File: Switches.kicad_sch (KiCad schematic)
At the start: 26 parts, among them Q10 POWER_FET, Q11 POWER_FET, Q12 POWER_FET, Q7 POWER_FET, Q8 POWER_FET, Q9 POWER_FET

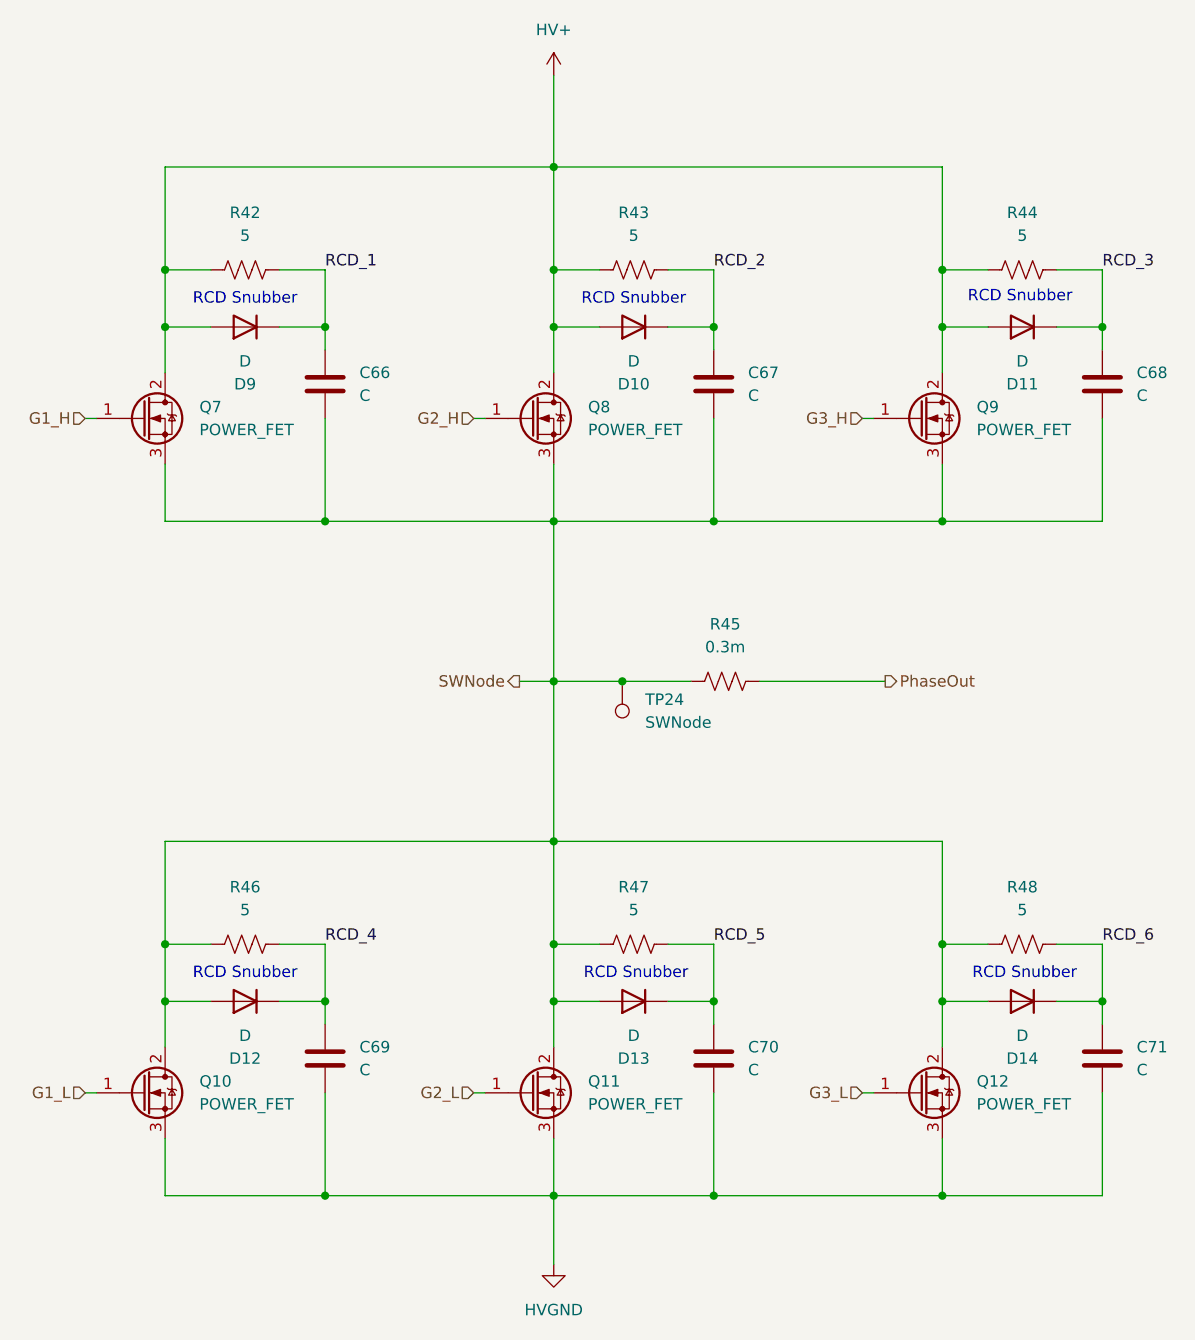
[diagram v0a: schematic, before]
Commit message: new bulk caps, new HV+,- connector placement
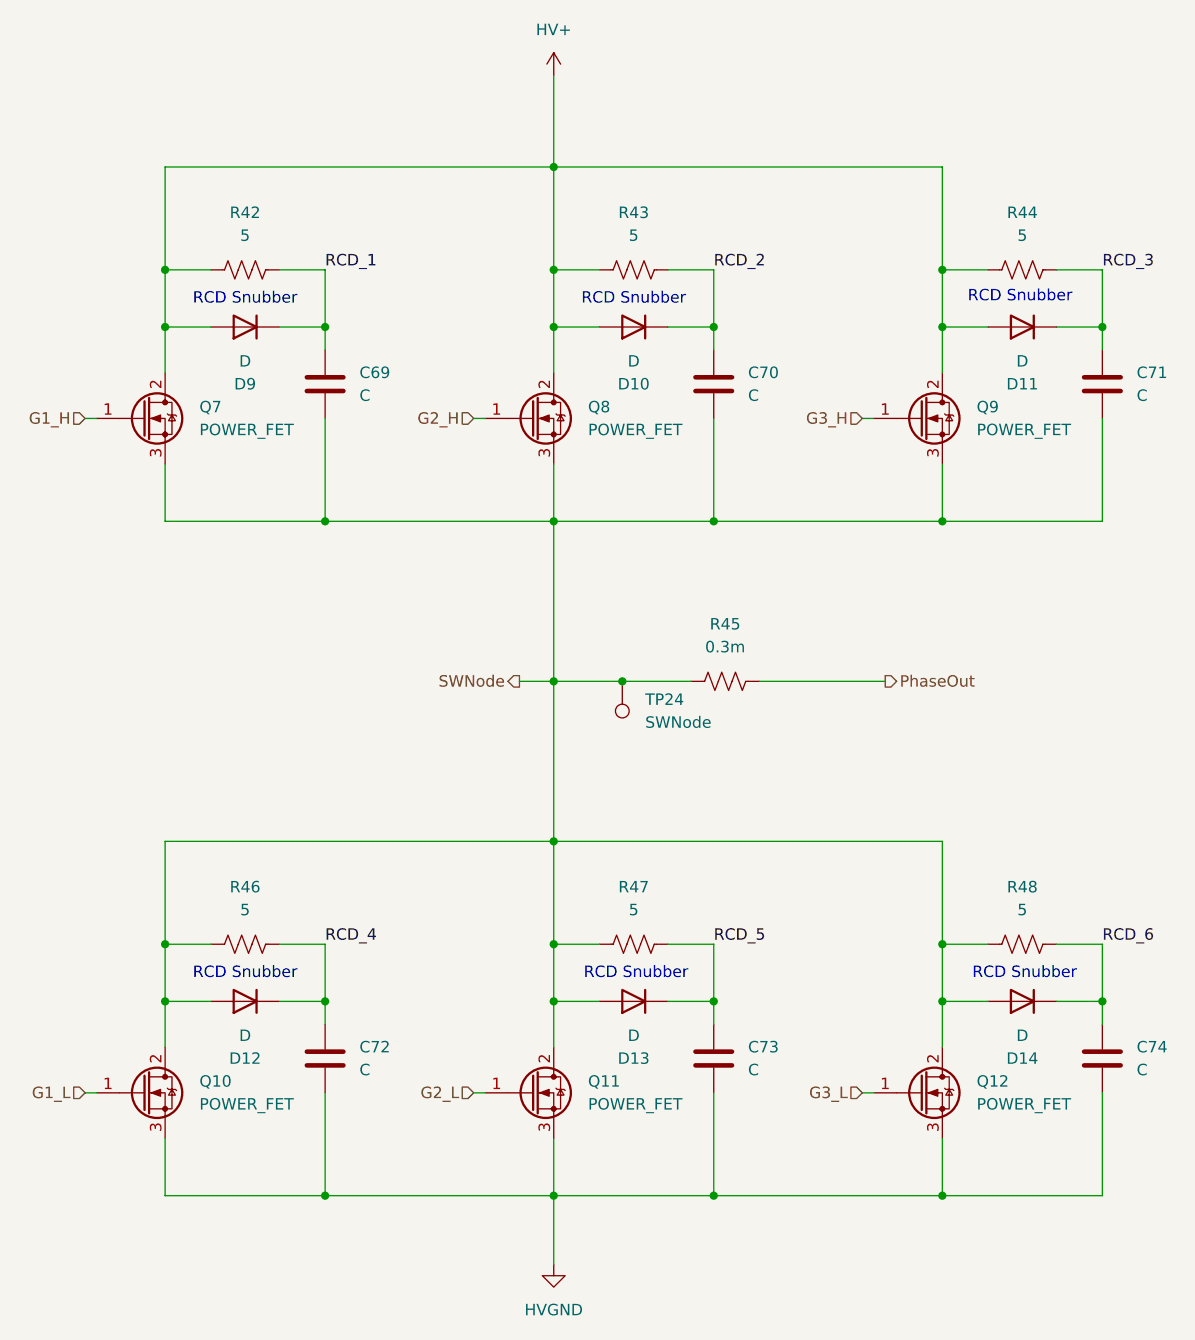
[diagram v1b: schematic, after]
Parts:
- renumbered C66 to C69, C67 to C70, C68 to C71, C69 to C72, C70 to C73, C71 to C74
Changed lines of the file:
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@@
 				)
 				(path "/bc91ffbf-afc6-42bb-9d28-6a3fecc21fcc/ebf1904e-ffdd-4ce1-98fa-2546468af80b/8a53f8a7-4fee-45b0-8115-af4354d69d86/61f5303a-4fdd-407b-8b75-bd44ef1dd029"
-					(reference "#PWR0175")
-					(unit 1)
-				)
-				(path "/bc91ffbf-afc6-42bb-9d28-6a3fecc21fcc/f1a23dc8-fe65-401e-b36f-fdc2d19203b3/8a53f8a7-4fee-45b0-8115-af4354d69d86/61f5303a-4fdd-407b-8b75-bd44ef1dd029"
-					(reference "#PWR0104")
+					(reference "#PWR0163")
+					(unit 1)
+				)
+				(path "/bc91ffbf-afc6-42bb-9d28-6a3fecc21fcc/f1a23dc8-fe65-401e-b36f-fdc2d19203b3/8a53f8a7-4fee-45b0-8115-af4354d69d86/61f5303a-4fdd-407b-8b75-bd44ef1dd029"
+					(reference "#PWR098")
 					(unit 1)
 				)
@@
 				)
 				(path "/bc91ffbf-afc6-42bb-9d28-6a3fecc21fcc/ebf1904e-ffdd-4ce1-98fa-2546468af80b/8a53f8a7-4fee-45b0-8115-af4354d69d86/61f5303a-4fdd-407b-8b75-bd44ef1dd029"
-					(reference "#PWR0176")
-					(unit 1)
-				)
-				(path "/bc91ffbf-afc6-42bb-9d28-6a3fecc21fcc/f1a23dc8-fe65-401e-b36f-fdc2d19203b3/8a53f8a7-4fee-45b0-8115-af4354d69d86/61f5303a-4fdd-407b-8b75-bd44ef1dd029"
-					(reference "#PWR0105")
+					(reference "#PWR0164")
+					(unit 1)
+				)
+				(path "/bc91ffbf-afc6-42bb-9d28-6a3fecc21fcc/f1a23dc8-fe65-401e-b36f-fdc2d19203b3/8a53f8a7-4fee-45b0-8115-af4354d69d86/61f5303a-4fdd-407b-8b75-bd44ef1dd029"
+					(reference "#PWR099")
 					(unit 1)
 				)
@@
 		(dnp no)
 		(fields_autoplaced yes)
-		(property "Reference" "C67"
+		(property "Reference" "C70"
 			(at 157.48 62.2299 0)
 			(effects
@@
 			(project "TractionInverter"
 				(path "/bc91ffbf-afc6-42bb-9d28-6a3fecc21fcc/3f7f1099-e875-4a86-860c-ef7a3936f734/8a53f8a7-4fee-45b0-8115-af4354d69d86/61f5303a-4fdd-407b-8b75-bd44ef1dd029"
-					(reference "C67")
-					(unit 1)
-				)
-				(path "/bc91ffbf-afc6-42bb-9d28-6a3fecc21fcc/ebf1904e-ffdd-4ce1-98fa-2546468af80b/8a53f8a7-4fee-45b0-8115-af4354d69d86/61f5303a-4fdd-407b-8b75-bd44ef1dd029"
-					(reference "C121")
-					(unit 1)
-				)
-				(path "/bc91ffbf-afc6-42bb-9d28-6a3fecc21fcc/f1a23dc8-fe65-401e-b36f-fdc2d19203b3/8a53f8a7-4fee-45b0-8115-af4354d69d86/61f5303a-4fdd-407b-8b75-bd44ef1dd029"
-					(reference "C75")
+					(reference "C70")
+					(unit 1)
+				)
+				(path "/bc91ffbf-afc6-42bb-9d28-6a3fecc21fcc/ebf1904e-ffdd-4ce1-98fa-2546468af80b/8a53f8a7-4fee-45b0-8115-af4354d69d86/61f5303a-4fdd-407b-8b75-bd44ef1dd029"
+					(reference "C124")
+					(unit 1)
+				)
+				(path "/bc91ffbf-afc6-42bb-9d28-6a3fecc21fcc/f1a23dc8-fe65-401e-b36f-fdc2d19203b3/8a53f8a7-4fee-45b0-8115-af4354d69d86/61f5303a-4fdd-407b-8b75-bd44ef1dd029"
+					(reference "C78")
 					(unit 1)
 				)
@@
 		(dnp no)
 		(fields_autoplaced yes)
-		(property "Reference" "C69"
+		(property "Reference" "C72"
 			(at 114.3 137.1599 0)
 			(effects
@@
 			(project "TractionInverter"
 				(path "/bc91ffbf-afc6-42bb-9d28-6a3fecc21fcc/3f7f1099-e875-4a86-860c-ef7a3936f734/8a53f8a7-4fee-45b0-8115-af4354d69d86/61f5303a-4fdd-407b-8b75-bd44ef1dd029"
-					(reference "C69")
-					(unit 1)
-				)
-				(path "/bc91ffbf-afc6-42bb-9d28-6a3fecc21fcc/ebf1904e-ffdd-4ce1-98fa-2546468af80b/8a53f8a7-4fee-45b0-8115-af4354d69d86/61f5303a-4fdd-407b-8b75-bd44ef1dd029"
-					(reference "C123")
-					(unit 1)
-				)
-				(path "/bc91ffbf-afc6-42bb-9d28-6a3fecc21fcc/f1a23dc8-fe65-401e-b36f-fdc2d19203b3/8a53f8a7-4fee-45b0-8115-af4354d69d86/61f5303a-4fdd-407b-8b75-bd44ef1dd029"
-					(reference "C77")
+					(reference "C72")
+					(unit 1)
+				)
+				(path "/bc91ffbf-afc6-42bb-9d28-6a3fecc21fcc/ebf1904e-ffdd-4ce1-98fa-2546468af80b/8a53f8a7-4fee-45b0-8115-af4354d69d86/61f5303a-4fdd-407b-8b75-bd44ef1dd029"
+					(reference "C126")
+					(unit 1)
+				)
+				(path "/bc91ffbf-afc6-42bb-9d28-6a3fecc21fcc/f1a23dc8-fe65-401e-b36f-fdc2d19203b3/8a53f8a7-4fee-45b0-8115-af4354d69d86/61f5303a-4fdd-407b-8b75-bd44ef1dd029"
+					(reference "C80")
 					(unit 1)
 				)
@@
 		(dnp no)
 		(fields_autoplaced yes)
-		(property "Reference" "C71"
+		(property "Reference" "C74"
 			(at 200.66 137.1599 0)
 			(effects
@@
 			(project "TractionInverter"
 				(path "/bc91ffbf-afc6-42bb-9d28-6a3fecc21fcc/3f7f1099-e875-4a86-860c-ef7a3936f734/8a53f8a7-4fee-45b0-8115-af4354d69d86/61f5303a-4fdd-407b-8b75-bd44ef1dd029"
-					(reference "C71")
-					(unit 1)
-				)
-				(path "/bc91ffbf-afc6-42bb-9d28-6a3fecc21fcc/ebf1904e-ffdd-4ce1-98fa-2546468af80b/8a53f8a7-4fee-45b0-8115-af4354d69d86/61f5303a-4fdd-407b-8b75-bd44ef1dd029"
-					(reference "C125")
-					(unit 1)
-				)
-				(path "/bc91ffbf-afc6-42bb-9d28-6a3fecc21fcc/f1a23dc8-fe65-401e-b36f-fdc2d19203b3/8a53f8a7-4fee-45b0-8115-af4354d69d86/61f5303a-4fdd-407b-8b75-bd44ef1dd029"
-					(reference "C79")
+					(reference "C74")
+					(unit 1)
+				)
+				(path "/bc91ffbf-afc6-42bb-9d28-6a3fecc21fcc/ebf1904e-ffdd-4ce1-98fa-2546468af80b/8a53f8a7-4fee-45b0-8115-af4354d69d86/61f5303a-4fdd-407b-8b75-bd44ef1dd029"
+					(reference "C128")
+					(unit 1)
+				)
+				(path "/bc91ffbf-afc6-42bb-9d28-6a3fecc21fcc/f1a23dc8-fe65-401e-b36f-fdc2d19203b3/8a53f8a7-4fee-45b0-8115-af4354d69d86/61f5303a-4fdd-407b-8b75-bd44ef1dd029"
+					(reference "C82")
 					(unit 1)
 				)
@@
 		(dnp no)
 		(fields_autoplaced yes)
-		(property "Reference" "C68"
+		(property "Reference" "C71"
 			(at 200.66 62.2299 0)
 			(effects
@@
 			(project "TractionInverter"
 				(path "/bc91ffbf-afc6-42bb-9d28-6a3fecc21fcc/3f7f1099-e875-4a86-860c-ef7a3936f734/8a53f8a7-4fee-45b0-8115-af4354d69d86/61f5303a-4fdd-407b-8b75-bd44ef1dd029"
-					(reference "C68")
-					(unit 1)
-				)
-				(path "/bc91ffbf-afc6-42bb-9d28-6a3fecc21fcc/ebf1904e-ffdd-4ce1-98fa-2546468af80b/8a53f8a7-4fee-45b0-8115-af4354d69d86/61f5303a-4fdd-407b-8b75-bd44ef1dd029"
-					(reference "C122")
-					(unit 1)
-				)
-				(path "/bc91ffbf-afc6-42bb-9d28-6a3fecc21fcc/f1a23dc8-fe65-401e-b36f-fdc2d19203b3/8a53f8a7-4fee-45b0-8115-af4354d69d86/61f5303a-4fdd-407b-8b75-bd44ef1dd029"
-					(reference "C76")
+					(reference "C71")
+					(unit 1)
+				)
+				(path "/bc91ffbf-afc6-42bb-9d28-6a3fecc21fcc/ebf1904e-ffdd-4ce1-98fa-2546468af80b/8a53f8a7-4fee-45b0-8115-af4354d69d86/61f5303a-4fdd-407b-8b75-bd44ef1dd029"
+					(reference "C125")
+					(unit 1)
+				)
+				(path "/bc91ffbf-afc6-42bb-9d28-6a3fecc21fcc/f1a23dc8-fe65-401e-b36f-fdc2d19203b3/8a53f8a7-4fee-45b0-8115-af4354d69d86/61f5303a-4fdd-407b-8b75-bd44ef1dd029"
+					(reference "C79")
 					(unit 1)
 				)
@@
 		(dnp no)
 		(fields_autoplaced yes)
-		(property "Reference" "C66"
+		(property "Reference" "C69"
 			(at 114.3 62.2299 0)
 			(effects
@@
 			(project "TractionInverter"
 				(path "/bc91ffbf-afc6-42bb-9d28-6a3fecc21fcc/3f7f1099-e875-4a86-860c-ef7a3936f734/8a53f8a7-4fee-45b0-8115-af4354d69d86/61f5303a-4fdd-407b-8b75-bd44ef1dd029"
-					(reference "C66")
-					(unit 1)
-				)
-				(path "/bc91ffbf-afc6-42bb-9d28-6a3fecc21fcc/ebf1904e-ffdd-4ce1-98fa-2546468af80b/8a53f8a7-4fee-45b0-8115-af4354d69d86/61f5303a-4fdd-407b-8b75-bd44ef1dd029"
-					(reference "C120")
-					(unit 1)
-				)
-				(path "/bc91ffbf-afc6-42bb-9d28-6a3fecc21fcc/f1a23dc8-fe65-401e-b36f-fdc2d19203b3/8a53f8a7-4fee-45b0-8115-af4354d69d86/61f5303a-4fdd-407b-8b75-bd44ef1dd029"
-					(reference "C74")
+					(reference "C69")
+					(unit 1)
+				)
+				(path "/bc91ffbf-afc6-42bb-9d28-6a3fecc21fcc/ebf1904e-ffdd-4ce1-98fa-2546468af80b/8a53f8a7-4fee-45b0-8115-af4354d69d86/61f5303a-4fdd-407b-8b75-bd44ef1dd029"
+					(reference "C123")
+					(unit 1)
+				)
+				(path "/bc91ffbf-afc6-42bb-9d28-6a3fecc21fcc/f1a23dc8-fe65-401e-b36f-fdc2d19203b3/8a53f8a7-4fee-45b0-8115-af4354d69d86/61f5303a-4fdd-407b-8b75-bd44ef1dd029"
+					(reference "C77")
 					(unit 1)
 				)
@@
 		(dnp no)
 		(fields_autoplaced yes)
-		(property "Reference" "C70"
+		(property "Reference" "C73"
 			(at 157.48 137.1599 0)
 			(effects
@@
 			(project "TractionInverter"
 				(path "/bc91ffbf-afc6-42bb-9d28-6a3fecc21fcc/3f7f1099-e875-4a86-860c-ef7a3936f734/8a53f8a7-4fee-45b0-8115-af4354d69d86/61f5303a-4fdd-407b-8b75-bd44ef1dd029"
-					(reference "C70")
-					(unit 1)
-				)
-				(path "/bc91ffbf-afc6-42bb-9d28-6a3fecc21fcc/ebf1904e-ffdd-4ce1-98fa-2546468af80b/8a53f8a7-4fee-45b0-8115-af4354d69d86/61f5303a-4fdd-407b-8b75-bd44ef1dd029"
-					(reference "C124")
-					(unit 1)
-				)
-				(path "/bc91ffbf-afc6-42bb-9d28-6a3fecc21fcc/f1a23dc8-fe65-401e-b36f-fdc2d19203b3/8a53f8a7-4fee-45b0-8115-af4354d69d86/61f5303a-4fdd-407b-8b75-bd44ef1dd029"
-					(reference "C78")
-					(unit 1)
-				)
+					(reference "C73")
+					(unit 1)
+				)
+				(path "/bc91ffbf-afc6-42bb-9d28-6a3fecc21fcc/ebf1904e-ffdd-4ce1-98fa-2546468af80b/8a53f8a7-4fee-45b0-8115-af4354d69d86/61f5303a-4fdd-407b-8b75-bd44ef1dd029"
+					(reference "C127")
+					(unit 1)
+				)
+				(path "/bc91ffbf-afc6-42bb-9d28-6a3fecc21fcc/f1a23dc8-fe65-401e-b36f-fdc2d19203b3/8a53f8a7-4fee-45b0-8115-af4354d69d86/61f5303a-4fdd-407b-8b75-bd44ef1dd029"
+					(reference "C81")
+					(unit 1)
+				)

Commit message: killed testpoints
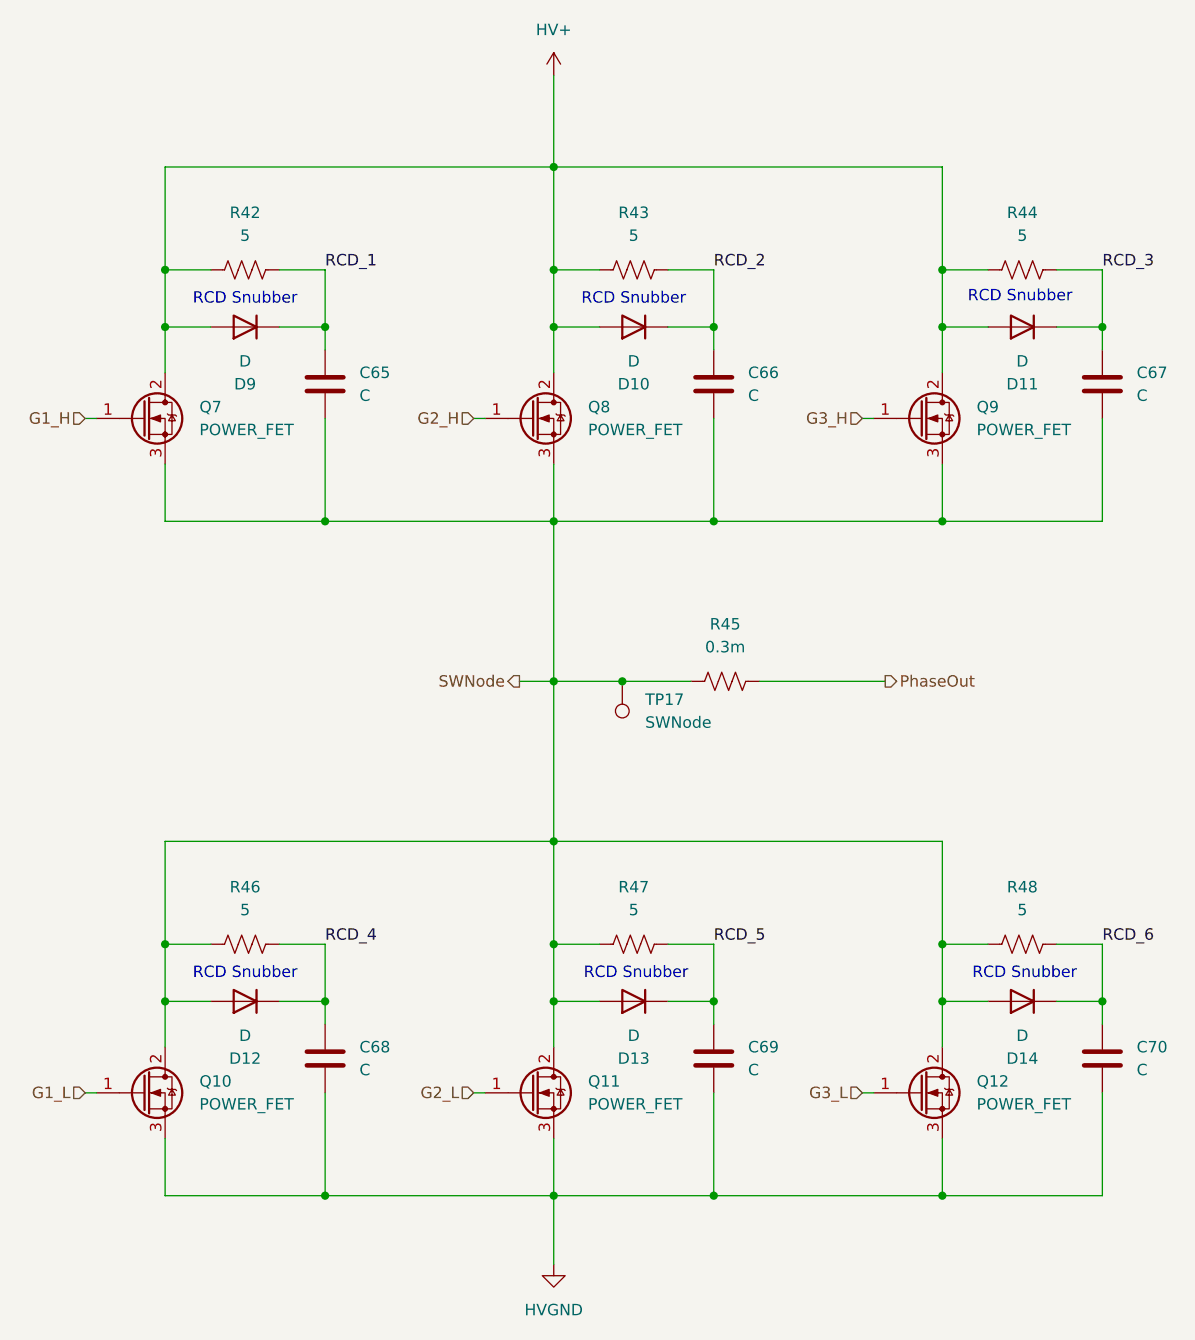
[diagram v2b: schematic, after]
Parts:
- renumbered C69 to C65, C70 to C66, C71 to C67, C72 to C68, C73 to C69, C74 to C70, TP24 to TP17

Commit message: need to pass drc
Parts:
- renumbered TP17 to TP21
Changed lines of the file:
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@@
 		(dnp no)
 		(fields_autoplaced yes)
-		(property "Reference" "TP17"
+		(property "Reference" "TP21"
 			(at 146.05 98.5519 0)
 			(effects
@@
 			(project "TractionInverter"
 				(path "/bc91ffbf-afc6-42bb-9d28-6a3fecc21fcc/3f7f1099-e875-4a86-860c-ef7a3936f734/8a53f8a7-4fee-45b0-8115-af4354d69d86/61f5303a-4fdd-407b-8b75-bd44ef1dd029"
-					(reference "TP17")
+					(reference "TP21")
 					(unit 1)
 				)
 				(path "/bc91ffbf-afc6-42bb-9d28-6a3fecc21fcc/ebf1904e-ffdd-4ce1-98fa-2546468af80b/8a53f8a7-4fee-45b0-8115-af4354d69d86/61f5303a-4fdd-407b-8b75-bd44ef1dd029"
-					(reference "TP33")
+					(reference "TP37")
 					(unit 1)
 				)
 				(path "/bc91ffbf-afc6-42bb-9d28-6a3fecc21fcc/f1a23dc8-fe65-401e-b36f-fdc2d19203b3/8a53f8a7-4fee-45b0-8115-af4354d69d86/61f5303a-4fdd-407b-8b75-bd44ef1dd029"
-					(reference "TP18")
+					(reference "TP22")
 					(unit 1)
 				)
